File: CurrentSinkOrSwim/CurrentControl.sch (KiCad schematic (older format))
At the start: 7 parts, among them Q301 BUK7575, U201 LMV358

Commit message: creado footprint heatsink
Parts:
- added P301: CONN_1, symbol CONN_1
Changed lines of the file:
@@
 Sheet 3 4
 Title ""
-Date "6 sep 2015"
+Date "7 sep 2015"
 Rev ""
 Comp ""
@@
 Curent_Sink-
 Connection ~ 8050 5800
+$Comp
+L CONN_1 P301
+U 1 1 55EDB470
+P 8900 3900
+F 0 "P301" H 8980 3900 40  0000 L CNN
+F 1 "CONN_1" H 8900 3955 30  0001 C CNN
+F 2 "" H 8900 3900 60  0000 C CNN
+F 3 "" H 8900 3900 60  0000 C CNN
+	1    8900 3900
+	1    0    0    -1
+$EndComp
 $EndSCHEMATC

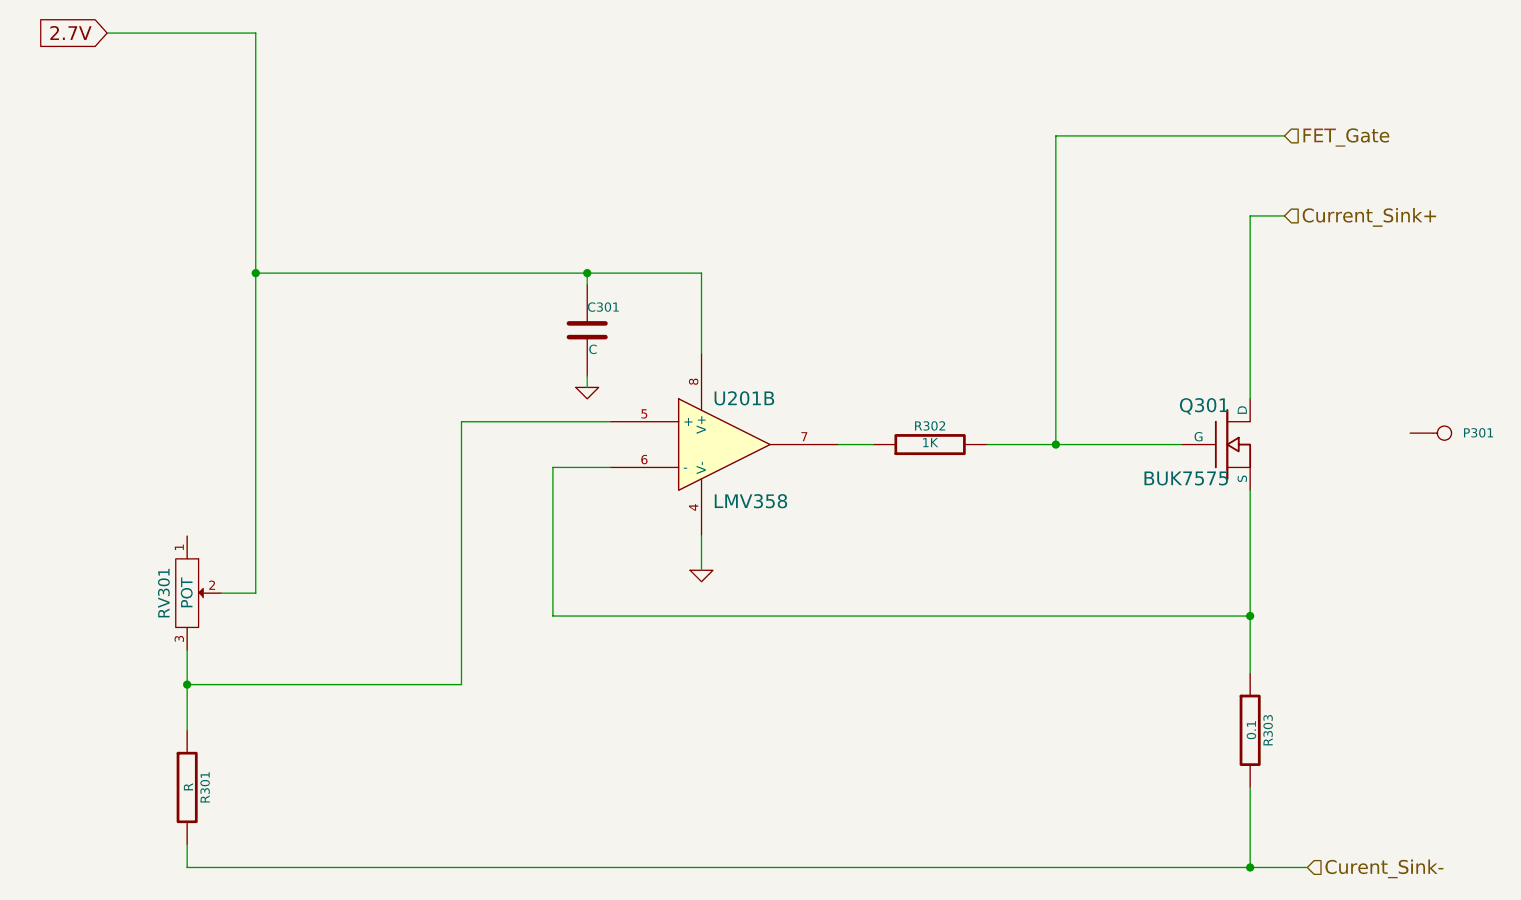
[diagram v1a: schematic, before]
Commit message: cambiando potenciómetro y divisores de tension
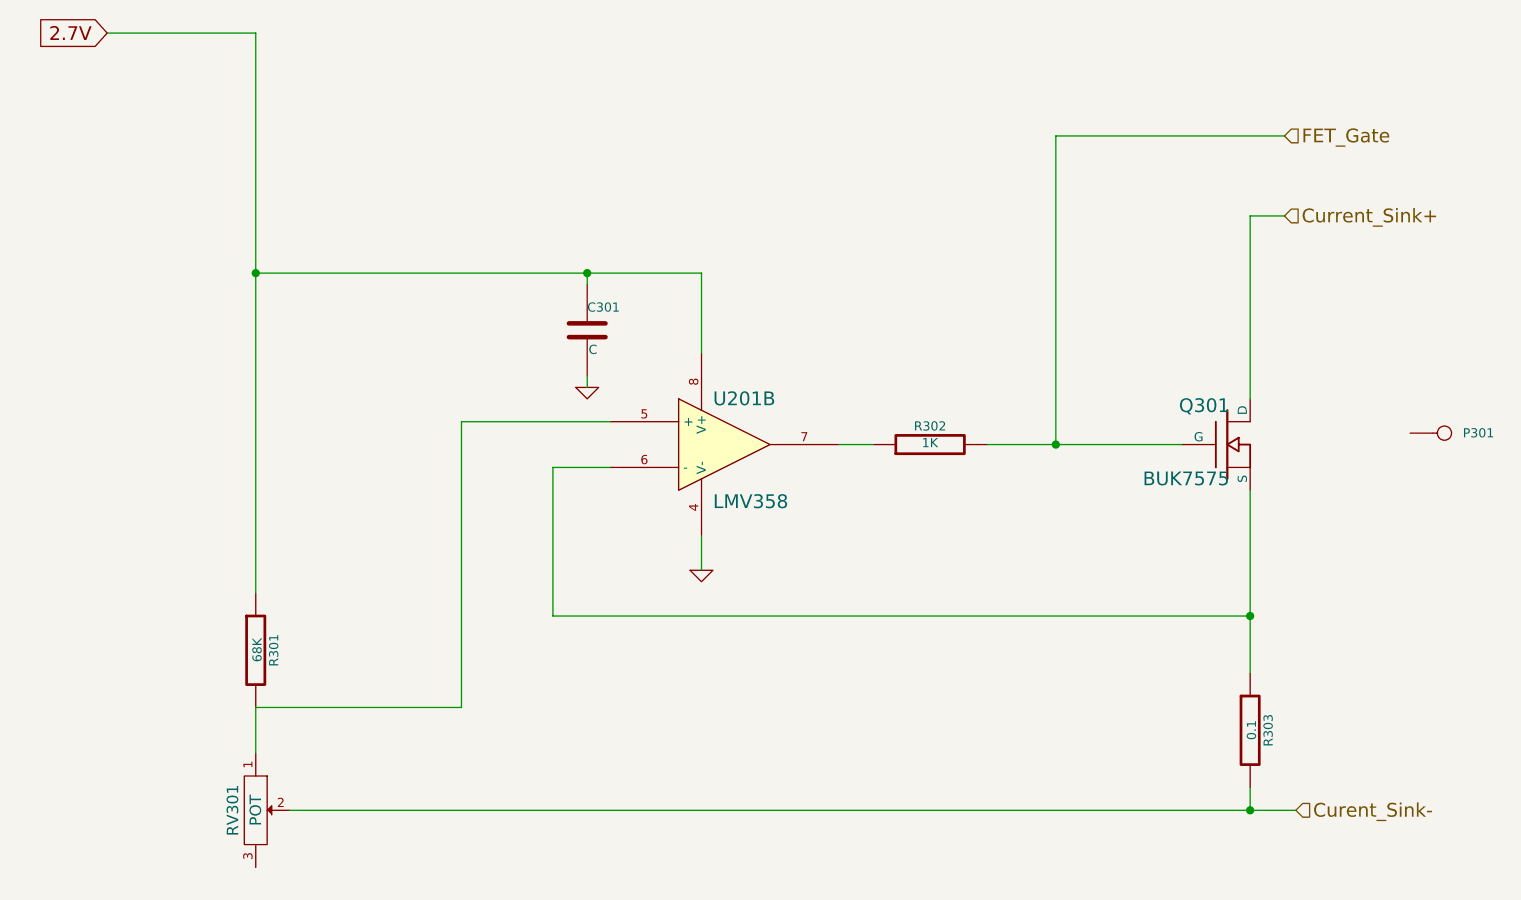
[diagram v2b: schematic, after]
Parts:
- R301: value R -> 68K
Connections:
- net 2.7V: now also R301.1; no longer RV301.2
- net Curent_Sink-: now also RV301.2; no longer R301.2
- net at RV301.1: now also R301.2, U201.5 (+)
- now unconnected: RV301.3
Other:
- moved on the sheet: R301, RV301
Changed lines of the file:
@@
 Sheet 3 4
 Title ""
-Date "7 sep 2015"
+Date "19 sep 2015"
 Rev ""
 Comp ""
@@
 L R R301
 U 1 1 55E5E18B
-P 3400 5450
-F 0 "R301" V 3480 5450 40  0000 C CNN
-F 1 "R" V 3407 5451 40  0000 C CNN
-F 2 "~" V 3330 5450 30  0000 C CNN
-F 3 "~" H 3400 5450 30  0000 C CNN
-	1    3400 5450
+P 3700 4850
+F 0 "R301" V 3780 4850 40  0000 C CNN
+F 1 "68K" V 3707 4851 40  0000 C CNN
+F 2 "~" V 3630 4850 30  0000 C CNN
+F 3 "~" H 3700 4850 30  0000 C CNN
+	1    3700 4850
 	1    0    0    -1
 $EndComp
@@
 L POT RV301
 U 1 1 55E5E197
-P 3400 4600
-F 0 "RV301" H 3400 4500 50  0000 C CNN
-F 1 "POT" H 3400 4600 50  0000 C CNN
-F 2 "~" H 3400 4600 60  0000 C CNN
-F 3 "~" H 3400 4600 60  0000 C CNN
-	1    3400 4600
+P 3700 5550
+F 0 "RV301" H 3700 5450 50  0000 C CNN
+F 1 "POT" H 3700 5550 50  0000 C CNN
+F 2 "~" H 3700 5550 60  0000 C CNN
+F 3 "~" H 3700 5550 60  0000 C CNN
+	1    3700 5550
 	0    1    1    0
 $EndComp
@@
 	5650 4350 5650 4500
 Wire Wire Line
-	3400 4850 3400 5200
-Wire Wire Line
 	5250 4050 5000 4050
 Wire Wire Line
@@
 	5250 3850 4600 3850
 Wire Wire Line
-	4600 3850 4600 5000
-Wire Wire Line
-	4600 5000 3400 5000
-Connection ~ 3400 5000
-Wire Wire Line
-	3400 5700 3400 5800
-Wire Wire Line
-	3400 5800 8300 5800
-Wire Wire Line
-	3700 4600 3550 4600
+	4600 3850 4600 5100
 Wire Wire Line
 	5650 3200 5650 3550
@@
 	5000 4700 8050 4700
 Connection ~ 8050 4700
-Wire Wire Line
-	8050 5800 8050 5450
 Text GLabel 3050 2150 0    60   Input ~ 0
 2.7V
@@
 Text HLabel 8200 2600 2    60   Input ~ 0
 FET_Gate
-Text HLabel 8300 5800 2    60   Input ~ 0
+Text HLabel 8250 5550 2    60   Input ~ 0
 Curent_Sink-
-Connection ~ 8050 5800
 $Comp
 L CONN_1 P301
@@
 	1    0    0    -1
 $EndComp
+Wire Wire Line
+	4600 5100 3700 5100
+Wire Wire Line
+	3700 5100 3700 5300
+Wire Wire Line
+	3850 5550 8250 5550
+Wire Wire Line
+	8050 5550 8050 5450
+Connection ~ 8050 5550
 $EndSCHEMATC

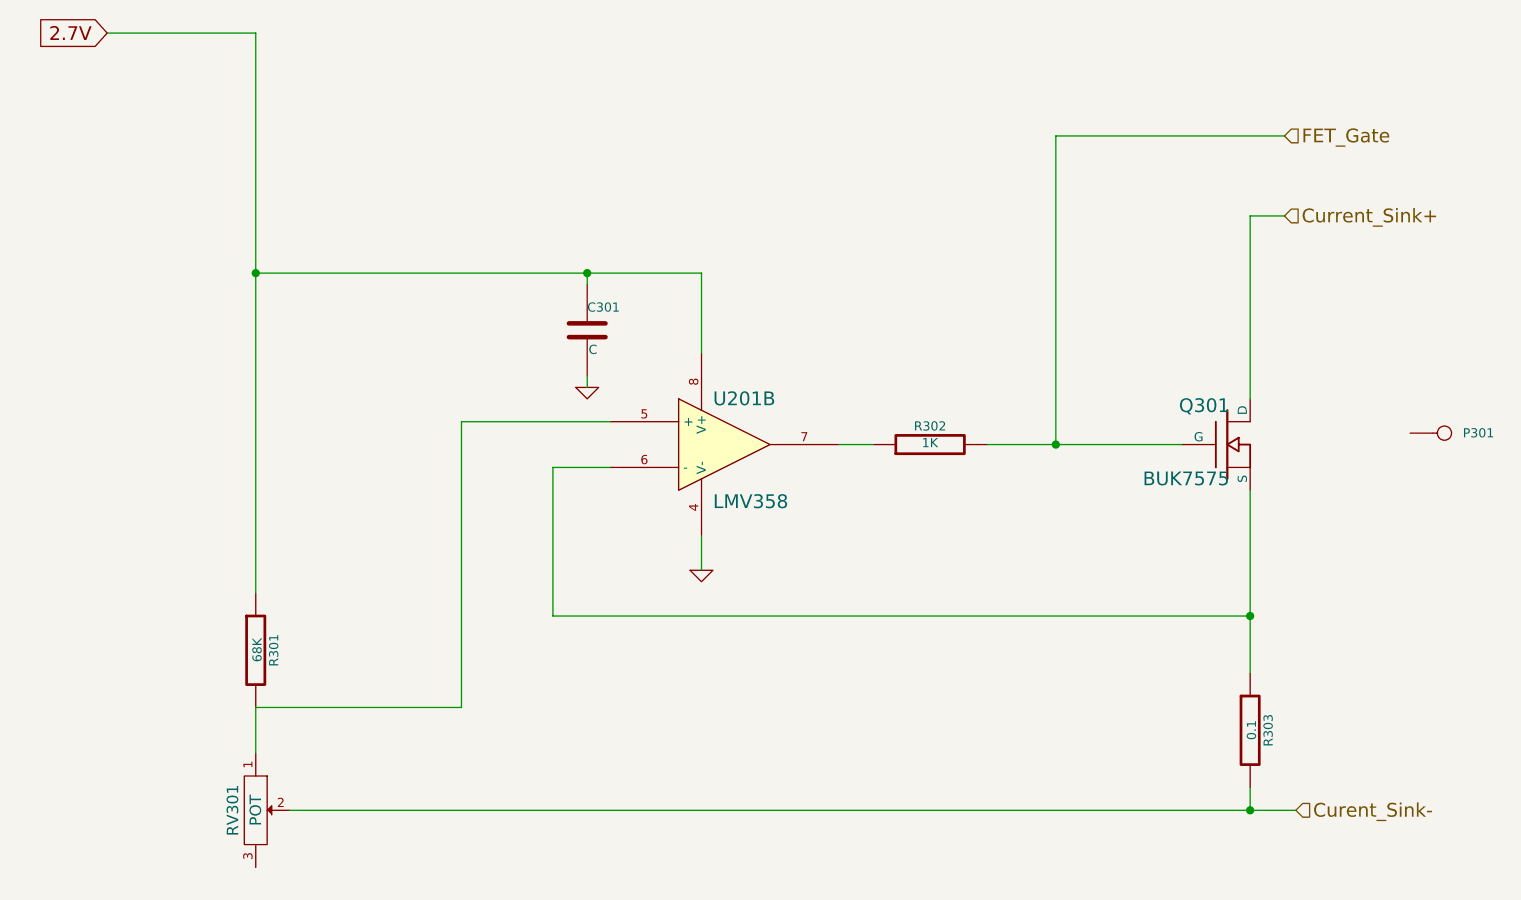
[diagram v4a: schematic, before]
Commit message: Actualizando información de los componentes y creando el BOM
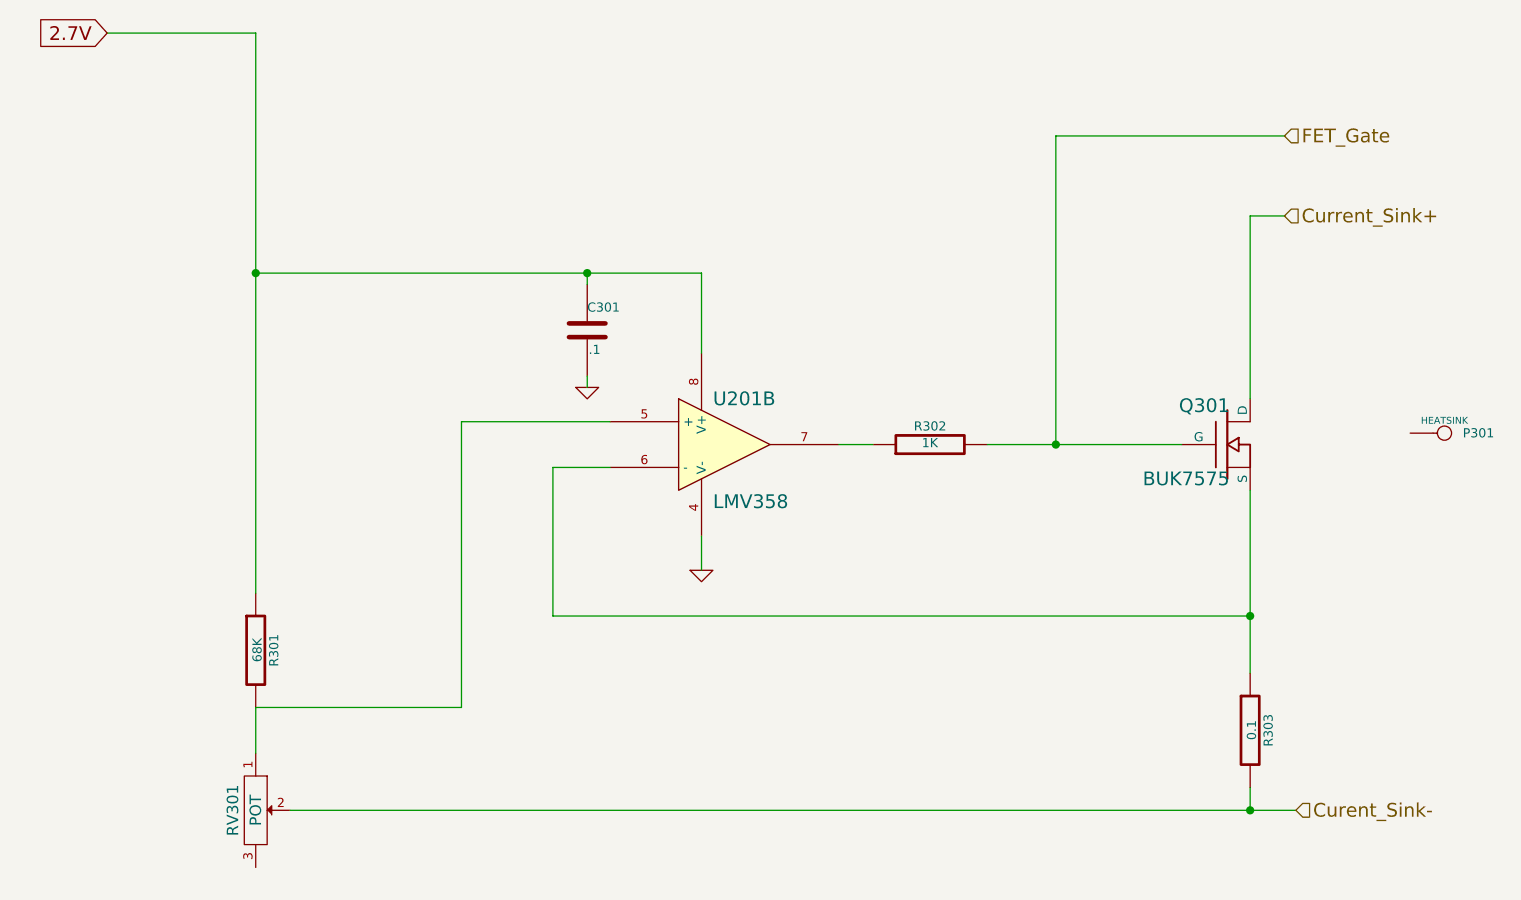
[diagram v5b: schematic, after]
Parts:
- C301: value C -> .1
- P301: value CONN_1 -> HEATSINK; MFG Name (none) -> FA-T220-38E
- RV301: MFG Name (none) -> ALPS 29 0001 POTENCIOMETRO
- U201: MFG Name (none) -> LMV358ID
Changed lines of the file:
@@
 Sheet 3 4
 Title ""
-Date "24 sep 2015"
+Date "1 oct 2015"
 Rev ""
 Comp ""
@@
 F 2 "" H 5750 3950 60  0000 C CNN
 F 3 "" H 5750 3950 60  0000 C CNN
+F 4 "LMV358ID" H 5750 3950 60  0001 C CNN "MFG Name"
 	2    5750 3950
 	1    0    0    -1
@@
 F 2 "~" H 3700 5550 60  0000 C CNN
 F 3 "~" H 3700 5550 60  0000 C CNN
+F 4 "ALPS 29 0001  POTENCIOMETRO" H 3700 5550 60  0001 C CNN "MFG Name"
 	1    3700 5550
 	0    1    1    0
@@
 P 5150 3450
 F 0 "C301" H 5150 3550 40  0000 L CNN
-F 1 "C" H 5156 3365 40  0000 L CNN
+F 1 ".1" H 5156 3365 40  0000 L CNN
 F 2 "~" H 5188 3300 30  0000 C CNN
 F 3 "~" H 5150 3450 60  0000 C CNN
@@
 P 8900 3900
 F 0 "P301" H 8980 3900 40  0000 L CNN
-F 1 "CONN_1" H 8900 3955 30  0001 C CNN
+F 1 "HEATSINK" H 8900 3955 30  0000 C CNN
 F 2 "" H 8900 3900 60  0000 C CNN
 F 3 "" H 8900 3900 60  0000 C CNN
+F 4 "FA-T220-38E" H 8900 3900 60  0001 C CNN "MFG Name"
 	1    8900 3900
 	1    0    0    -1

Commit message: Haciendo algunos cambios porque he tenido que cambiar de componentes y algún valor estaba mal
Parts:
- P301: MFG Name FA-T220-38E -> 637-10ABEP
- R303: MFG Part Number AC01000001007JA100 -> LVR01R1000FE12
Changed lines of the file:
@@
 Sheet 3 4
 Title ""
-Date "1 oct 2015"
+Date "5 oct 2015"
 Rev ""
 Comp ""
@@
 F 2 "~" V 7980 5200 30  0000 C CNN
 F 3 "~" H 8050 5200 30  0000 C CNN
-F 4 "AC01000001007JA100" H 8050 5200 60  0001 C CNN "MFG Part Number"
+F 4 "LVR01R1000FE12" H 8050 5200 60  0001 C CNN "MFG Part Number"
 	1    8050 5200
 	1    0    0    -1
@@
 F 2 "" H 8900 3900 60  0000 C CNN
 F 3 "" H 8900 3900 60  0000 C CNN
-F 4 "FA-T220-38E" H 8900 3900 60  0001 C CNN "MFG Name"
+F 4 "637-10ABEP" H 8900 3900 60  0001 C CNN "MFG Name"
 	1    8900 3900
 	1    0    0    -1
